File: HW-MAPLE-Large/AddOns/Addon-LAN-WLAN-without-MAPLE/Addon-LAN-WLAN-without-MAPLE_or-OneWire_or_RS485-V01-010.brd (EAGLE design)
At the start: 49 x 57.2 mm, 32 parts, among them IC1 LD117ADT50TR, IC2 DS2480B, IC6 LM1117MPX-ADJ, M1 ARDUINO-PRO-MINI-3.3V#NP, X4 1751248, X7 1751264

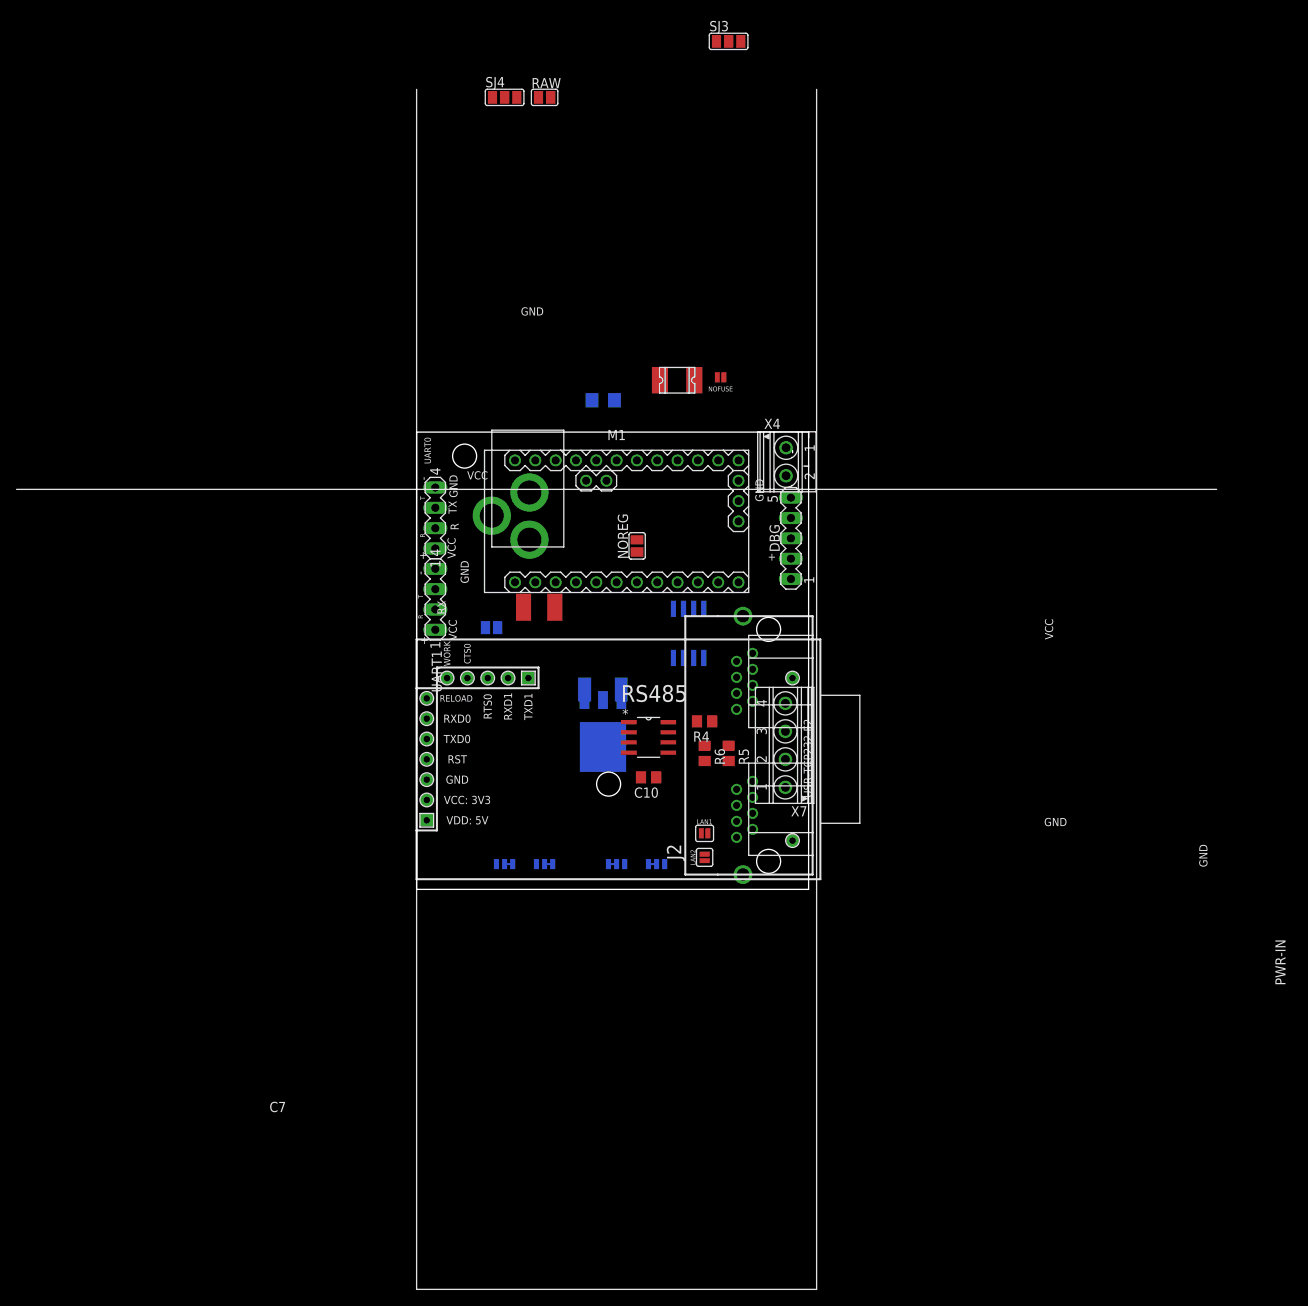
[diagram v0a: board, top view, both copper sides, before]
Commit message: 1W-UART
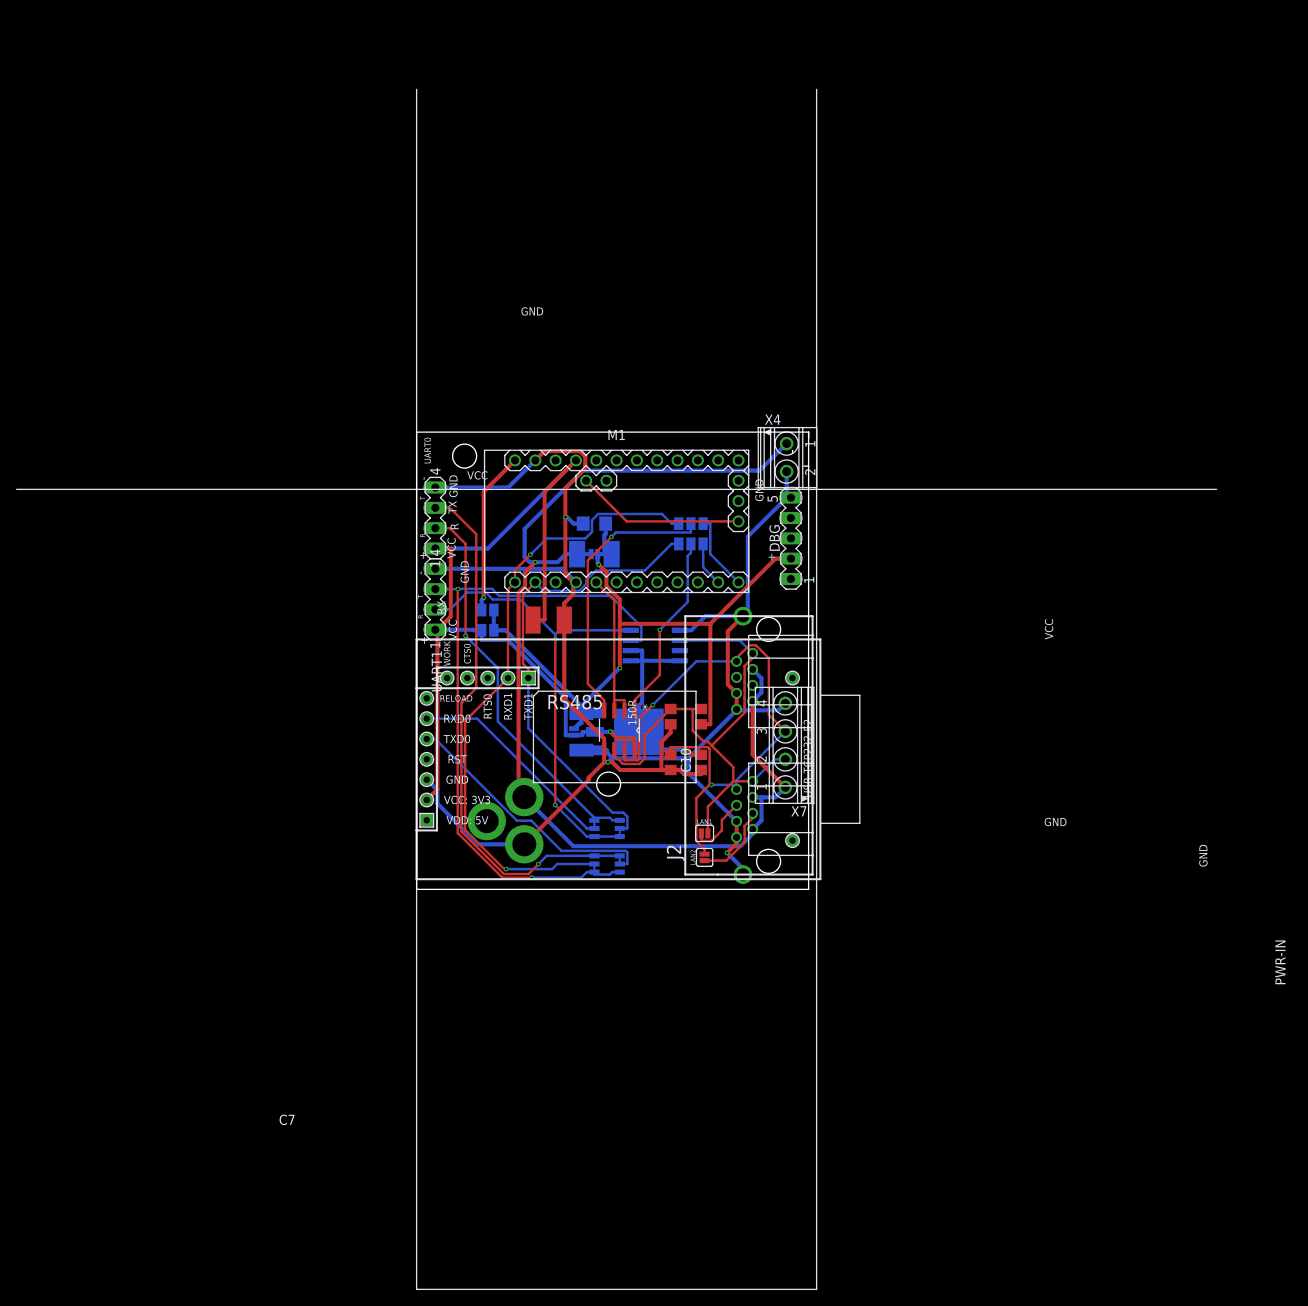
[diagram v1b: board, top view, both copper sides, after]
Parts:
- removed SJ3, SJ4: (no value), jumper:SJ_2
- added RX, TX: (no value), jumper:SJ_2
- NOREG: value (none) -> JUMPER-SMT_2_NC_PASTE_NO-SILK; device jumper:SJ -> SparkFun-Jumpers:SMT-JUMPER_2_NC_PASTE_NO-SILK
- R4: value 150R -> 5K6
- R5: value 330R -> 22K
- R6: value 330R -> 4K7
- moved RAW 64.5 mm to (8.89, 34.9), flipped to the bottom, turned to 180 degrees
- moved U$2 50.8 mm to (13.4, 2.25), flipped to the bottom, turned to 180 degrees
- moved NOFUSE 27.1 mm to (22.2, 41.9), flipped to the bottom, turned to 0 degrees
- moved NOREG 24.5 mm to (19.7, 19.7), flipped to the bottom
- moved F1 24.1 mm to (22.2, 41.9), flipped to the bottom, turned to 0 degrees
- moved C9 15.4 mm to (22.2, 45.7)
- moved TX_SEL 15.1 mm to (25.4, 7.62), turned to 270 degrees
- moved TX_1 8.96 mm to (22.2, 7.62), turned to 90 degrees
- moved C10 6.82 mm to (35.6, 15.9), turned to 90 degrees
- moved RX_SEL 6.23 mm to (22.2, 3.17), turned to 270 degrees
- moved R5 5.74 mm to (35.6, 21.6), turned to 90 degrees
- moved IC2 4.42 mm to (29.8, 30.5), turned to 270 degrees
- moved R6 4.40 mm to (31.8, 15.9)
- moved R4 4.29 mm to (31.8, 21.6), turned to 90 degrees
- moved RS485 3.76 mm to (25.4, 19.9), turned to 270 degrees
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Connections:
- net A: now also R4.2; no longer R4.1
- net B: no longer R4.2
- net D8: now also RX.3; no longer SJ3.3
- net D9: now also TX.3; no longer SJ4.3
- net DI1: now also TX.2; no longer SJ4.2
- net GND: now also R4.1
- net IN: now also R5.1
- net RO: now also RX.2; no longer SJ3.2
- net RX: now also RX.1; no longer SJ3.1
- net TX: now also TX.1; no longer SJ4.1
- net VCC: no longer R5.1
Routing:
- net GND: track 0.00 -> 225.4 mm, vias 0 -> 3
- net VCC: track 0.00 -> 147.7 mm, vias 0 -> 2
- net VIN: track 0.00 -> 138.9 mm, vias 0 -> 1
- net IN: track 0.00 -> 88.7 mm, vias 0 -> 2
- net RX1: track 0.00 -> 84.6 mm, vias 0 -> 2
- net TX: track 0.00 -> 78.3 mm, vias 0 -> 2
- net B: track 0.00 -> 72.5 mm, vias 0 -> 2
- net RX0: track 0.00 -> 67.4 mm, vias 0 -> 1
- net A: track 0.00 -> 66.9 mm
- net RX: track 0.00 -> 59.6 mm
- net TX1: track 0.00 -> 58.7 mm, vias 0 -> 2
- net TX0: track 0.00 -> 49.1 mm, vias 0 -> 1
- net DI1: track 0.00 -> 35.0 mm, vias 0 -> 1
- net USRTX0: track 0.00 -> 33.3 mm
- net USRRX0: track 0.00 -> 26.6 mm
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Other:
- board text added: "150R"
- board text added: "RS485"
